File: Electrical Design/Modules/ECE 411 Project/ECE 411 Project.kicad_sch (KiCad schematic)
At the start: 18 parts, among them J1 5mm 9V Barrel, J2 BOOST, U1 HT7333, U2 LT1054

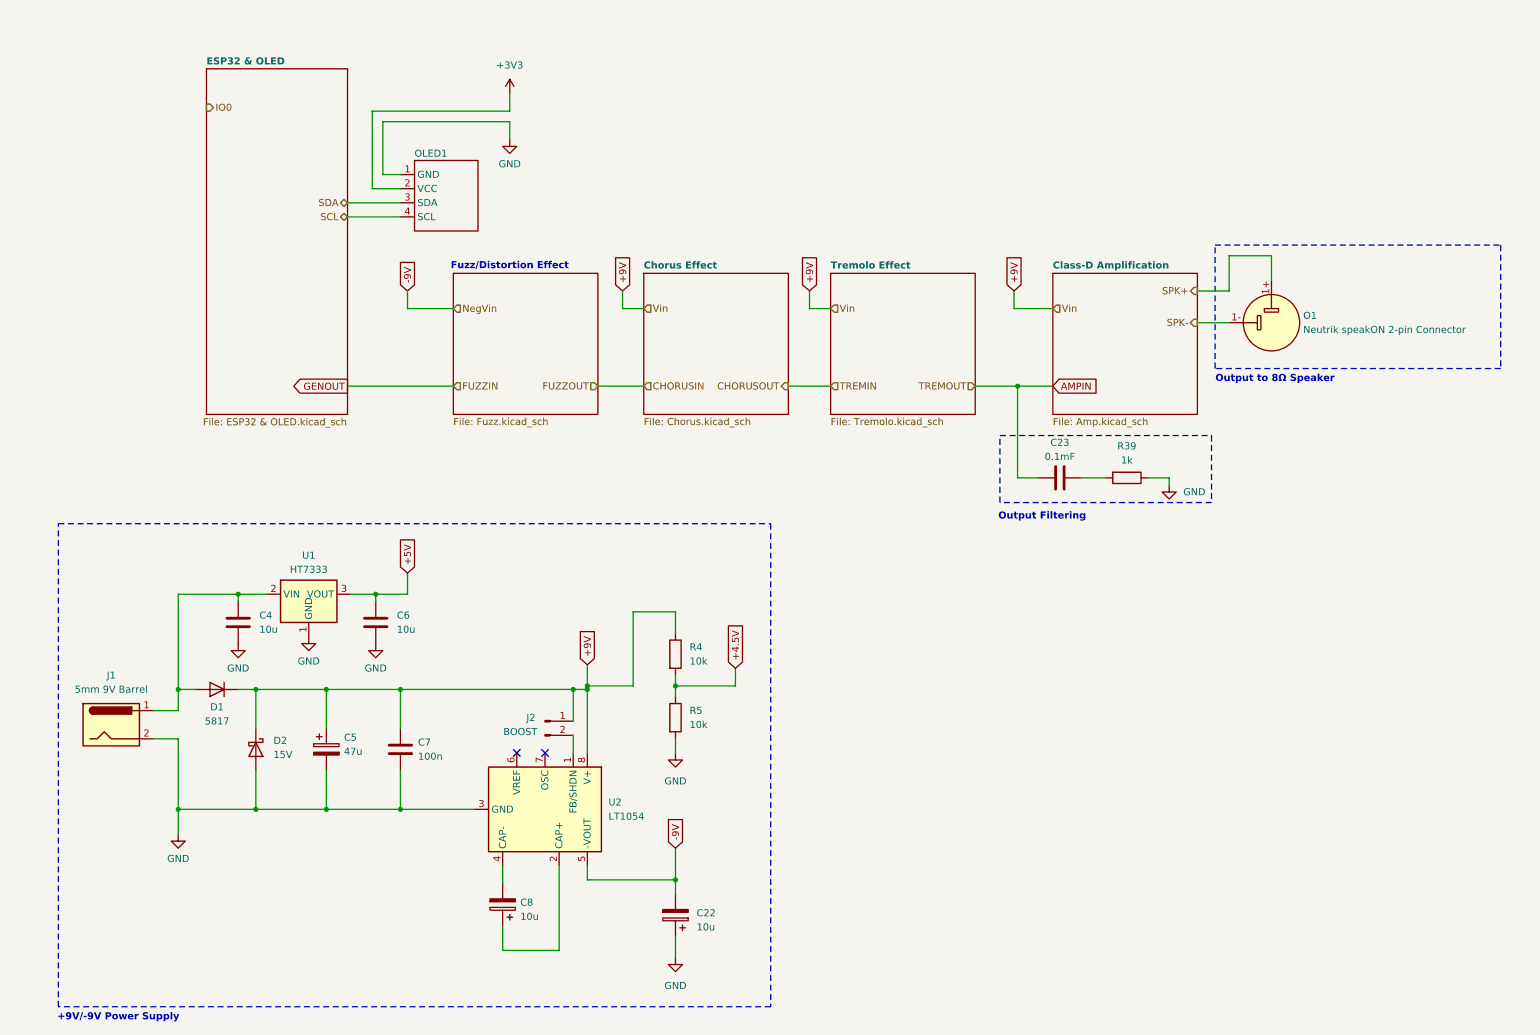
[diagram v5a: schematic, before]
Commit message: schematic, start layout
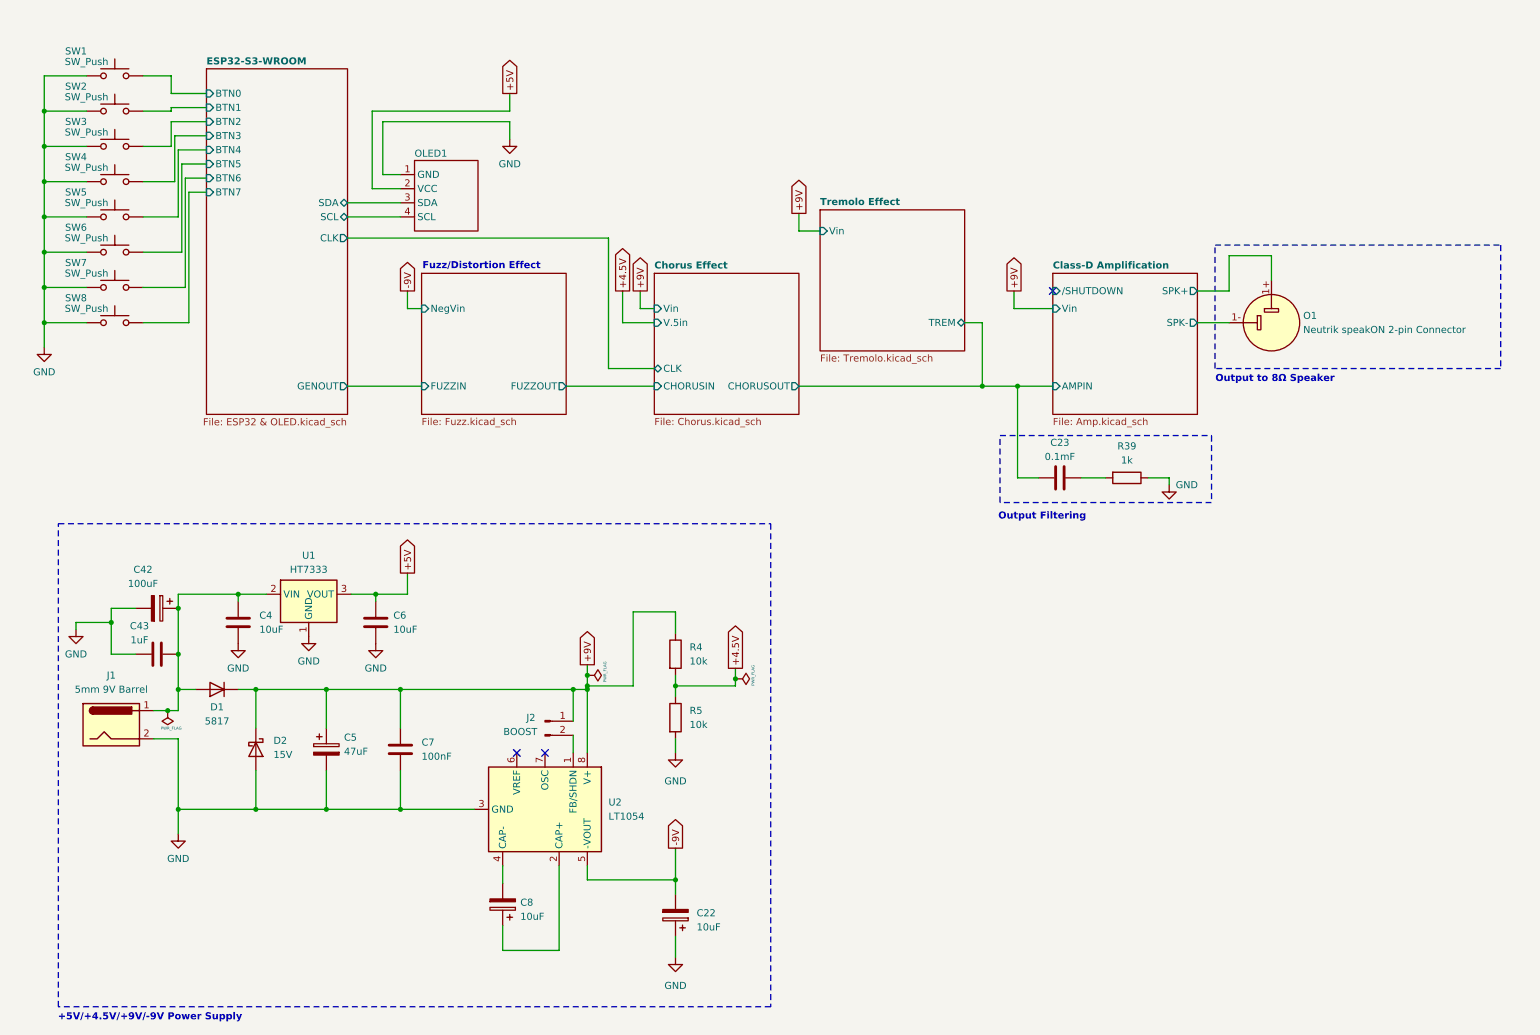
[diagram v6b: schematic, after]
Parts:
- added C42: 100uF, Capacitor_THT:CP_Radial_D6.3mm_P2.50mm, symbol Device:C_Polarized
- added C43: 1uF, Capacitor_SMD:C_0805_2012Metric_Pad1.18x1.45mm_HandSolder, symbol Device:C
- added SW1, SW2, SW3, SW4, SW5, SW6, SW7, SW8: SW_Push, Connector_PinHeader_2.54mm:PinHeader_1x02_P2.54mm_Vertical, symbol Switch:SW_Push
- C22: value 10u -> 10uF; footprint (none) -> Capacitor_THT:CP_Radial_D7.5mm_P2.50mm
- C23: footprint (none) -> Capacitor_SMD:C_0805_2012Metric_Pad1.18x1.45mm_HandSolder
- C4: value 10u -> 10uF; footprint (none) -> Capacitor_THT:C_Axial_L12.0mm_D6.5mm_P20.00mm_Horizontal
- C5: value 47u -> 47uF; footprint (none) -> Capacitor_THT:CP_Radial_D8.0mm_P3.50mm
- C6: value 10u -> 10uF; footprint (none) -> Capacitor_SMD:C_0805_2012Metric_Pad1.18x1.45mm_HandSolder
- C7: value 100n -> 100nF; footprint (none) -> Capacitor_SMD:C_0805_2012Metric_Pad1.18x1.45mm_HandSolder
- C8: value 10u -> 10uF; footprint (none) -> Capacitor_THT:CP_Radial_D8.0mm_P3.50mm
- D1, D2: footprint (none) -> Diode_SMD:D_0805_2012Metric_Pad1.15x1.40mm_HandSolder
- J1: footprint (none) -> Connector_BarrelJack:BarrelJack_Horizontal
- J2: footprint (none) -> Connector_PinHeader_2.54mm:PinHeader_1x02_P2.54mm_Horizontal
- O1: footprint (none) -> Connector_Audio:Jack_speakON_Neutrik_NL4MDXX-H-2_Horizontal
- OLED1: footprint (none) -> Connector_PinHeader_2.54mm:PinHeader_1x04_P2.54mm_Vertical
- R39, R4, R5: footprint (none) -> Resistor_SMD:R_0805_2012Metric_Pad1.20x1.40mm_HandSolder
- U2: footprint (none) -> Package_DIP:CERDIP-8_W7.62mm_SideBrazed
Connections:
- net +3V3 is gone; now on net +5V: OLED1.2 (VCC)
- net GND: now also C42.2, C43.1, SW1.1, SW2.1, SW3.1, SW4.1, SW5.1, SW6.1, SW7.1, SW8.1
- net at C4.1, D1.2 (A), J1.1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: now also C42.1, C43.2
- net AMPIN renamed Chorus Effect/CHORUSOUT
- net SCL renamed ESP32-S3-WROOM/SCL
- net SDA renamed ESP32-S3-WROOM/SDA
- net SPK+ renamed Class-D Amplification/SPK+
- net SPK- renamed Class-D Amplification/SPK-
- new net ESP32-S3-WROOM/BTN0: SW1.2
- new net ESP32-S3-WROOM/BTN1: SW2.2
- new net ESP32-S3-WROOM/BTN2: SW3.2
- new net ESP32-S3-WROOM/BTN3: SW4.2
- new net ESP32-S3-WROOM/BTN4: SW5.2
- new net ESP32-S3-WROOM/BTN5: SW6.2
- new net ESP32-S3-WROOM/BTN6: SW7.2
- new net ESP32-S3-WROOM/BTN7: SW8.2
- no-connect marks 2 -> 3
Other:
- sheet ESP32 & OLED renamed ESP32-S3-WROOM
- sheet Chorus Effect ports: added CHORUSIN, CHORUSOUT, CLK, V.5in, Vin; removed none
- sheet Class-D Amplification ports: added AMPIN, SPK+, SPK-, Vin, /SHUTDOWN; removed none
- sheet ESP32-S3-WROOM ports: added BTN0, BTN1, BTN2, BTN3, BTN4, BTN5, BTN6, BTN7, CLK, GENOUT, SCL, SDA; removed none
- sheet Fuzz Schematic ports: added FUZZIN, FUZZOUT, NegVin; removed none
- sheet Tremolo Effect ports: added TREM, Vin; removed none
- note added: "+5V/+4.5V/+9V/-9V Power Supply"
- note removed: "+9V/-9V Power Supply"

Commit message: update kicad
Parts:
- removed O1: Neutrik speakON 2-pin Connector, Connector_Audio:Jack_speakON_Neutrik_NL4MDXX-H-2_Horizontal, symbol Connector_Audio:SpeakON_NL2
- added J3: Pheonix Connector, 1190297:PHOENIX_1190297, symbol Pheonix-1190297:1190297
- added RV1, RV2, RV3: 10k, Connector_PinSocket_2.54mm:PinSocket_1x03_P2.54mm_Vertical, symbol Device:R_Potentiometer
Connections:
- net Chorus Effect/CHORUSIN: now also RV1.2, RV2.1
- net Chorus Effect/CHORUSOUT: now also RV2.2, RV3.1; no longer C23.1
- net Class-D Amplification/SPK+: now also J3.1_1, J3.1_2
- net Class-D Amplification/SPK-: now also J3.2_1, J3.2_2
- net ESP32-S3-WROOM/GENOUT: now also RV1.1
- new net Class-D Amplification/AMPIN: C23.1, RV3.2
- no-connect marks 3 -> 6
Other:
- sheet Tremolo Effect ports: added CLK, TREMIN, TREMOUT; removed TREM
- moved on the sheet: C23, R39

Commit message: update BOM
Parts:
- C22, C23, C42, C43, D1, D2, R39, R4, R5: Part Origin (none) -> DK
- C4: footprint Capacitor_THT:C_Axial_L12.0mm_D6.5mm_P20.00mm_Horizontal -> Capacitor_SMD:C_1206_3216Metric_Pad1.33x1.80mm_HandSolder; On Hand (On Way) (none) -> (100; Part Number (none) -> CL31B106KAHNFNE; Part Origin (none) -> DK
- C5: On Hand (On Way) (none) -> (15); Part Number (none) -> UVK2A470MPD; Part Origin (none) -> DK
- C6: footprint Capacitor_SMD:C_0805_2012Metric_Pad1.18x1.45mm_HandSolder -> Capacitor_SMD:C_1206_3216Metric_Pad1.33x1.80mm_HandSolder; On Hand (On Way) (none) -> (100; Part Number (none) -> CL31B106KAHNFNE; Part Origin (none) -> DK
- C7: value 100nF -> 0.1uF; On Hand (On Way) (none) -> (100); Part Number (none) -> CL21B104KCFNNNE; Part Origin (none) -> DK
- C8: On Hand (On Way) (none) -> (15); Part Number (none) -> UVR2C100MPD; Part Origin (none) -> DK
- RV1, RV2, RV3: Part Origin (none) -> AMZ
- SW1, SW2, SW3, SW4, SW5, SW6, SW7, SW8: Part Origin (none) -> TAYDA
- U1, U2: Part Origin (none) -> SBP
